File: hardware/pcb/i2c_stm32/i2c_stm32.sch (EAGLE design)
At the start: 41 parts, among them J1 POWER, Q1 16 MHz, Q2 32 MHz, Q3 8 MHz, U1 STM32F103C8T6, U2 MPU-6050, U3 BMP280, U4 NRF24L01

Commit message: Schematic finalized (besides crystal load c ap and resistor values)
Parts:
- removed C14: 10nF, Resistor_Capacitor:C0603C100C5GACTU
- removed C15: 1nF, Resistor_Capacitor:C0603C100C5GACTU
- removed C23: 100 nF, Resistor_Capacitor:C0603C100C5GACTU
- removed J1: POWER, SparkFun-Connectors:CONN_023.5MM
- removed JP1: (no value), adafruit:PINHD-1X6B
- removed JP2: (no value), adafruit:PINHD-1X8BIG
- removed LED1: (no value), led:LED5MM
- removed Q1: 16 MHz, adafruit:CRYSTALHC49S
- removed Q2: 32 MHz, adafruit:CRYSTALHC49S
- removed Q3: 8 MHz, adafruit:CRYSTALHC49S
- removed U$1: 2.7 nH, Nordic_nRF:INDUCTOR_0603_M
- removed U$2: 8.2 nH, Nordic_nRF:INDUCTOR_0603_M
- removed U$3: 3.9 nH, Nordic_nRF:INDUCTOR_0603_M
- added C24: 22nF, Resistor_Capacitor:C0603C100C5GACTU
- added C25, C27, C29: 100nF, Resistor_Capacitor:C0603C100C5GACTU
- added C26: 1uF, Resistor_Capacitor:C0603C100C5GACTU
- added C28: 10uF, Resistor_Capacitor:C0603C100C5GACTU
- added C30, C31: 22pF, Resistor_Capacitor:C0603C100C5GACTU
- added D1, D2: (no value), SparkFun-LED:LED0603
- added J2: (no value), SparkFun-Connectors:CONN_04
- added J3, J4: (no value), SparkFun-Connectors:CONN_20
- added J5: (no value), SparkFun-Connectors:USB_MICRO-B_FEMALE-SMT
- added L1: 2.7 nH, Nordic_nRF:INDUCTOR_0603_M
- added L2: 8.2 nH, Nordic_nRF:INDUCTOR_0603_M
- added L3: 3.9 nH, Nordic_nRF:INDUCTOR_0603_M
- added R4: RC0603JR-070RL, Resistor_Capacitor:RC0603JR-070RL
- added R5: 10k, Resistor_Capacitor:RC0603JR-070RL
- added S1: MOMENTARY-SWITCH-SPST-PTH-6.0MM, SparkFun-Switches:MOMENTARY-SWITCH-SPST-PTH-6.0MM
- added U5: RT9193-33GB, SparkFun-IC-Power:V_REG_MIC5205ADJ
- added Y1: 8MHz, SparkFun-Clocks:CRYSTAL-8MHZSMD-5X3.2
- added Y3: 16MHz, SparkFun-Clocks:CRYSTAL-16MHZSMD-5X3.2
- added Y4: 32.768kHz, SparkFun-Clocks:CRYSTAL-32.768KHZSMD-3.2X1.5
- C10: value 100 nF -> 1pF
- C16, C17: value 2.2nF -> 22pF
- C18, C19: value 2.2nF -> 100nF
- C20, C21: value 100 nF -> 100nF
- C22: value 100 nF -> 1uF
- C4: value 0.01 uF -> 0.01uF
- C9: value 100 nF -> 1.5pF
- R3: value 1 M -> 1M
- U1: SPICEPREFIX (none) -> X
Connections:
- removed net N$10: U$1.1, U$2.1, U4.ANT1
- removed net N$11: U$2.2, U$3.1, U4.ANT2
- removed net SCL: JP1.4, U2.SCL
- removed net SDA: JP1.3, U2.SDA, U3.SDI
- new net 5V: C25.2, C26.2, J4.3, J5.VBUS, U5.EN, U5.IN
- new net ANT1: L1.1, L2.1, U4.ANT1
- new net ANT2: L2.2, L3.1, U4.ANT2
- new net BMP_SCL: U3.BMP_SCK
- new net BMP_SDA: U3.SDI
- new net EP: U2.EP, U4.EP
- new net IMU_SCL: U2.SCL
- new net IMU_SDA: U2.SDA
- new net N$14: C25.1, C26.1, U5.GND
- new net N$15: U3.SDO
- new net OSC32_IN: C30.1, U1.PC14-OSC32_IN, Y4.1
- new net OSC32_OUT: C31.1, U1.PC15-OSC32_OUT, Y4.2
- new net OSC_IN: C16.1, R3.2, U1.PD0_OSC_IN, Y1.1
- new net OSC_OUT: C17.1, R3.1, U1.PD1_OSC_OUT, Y1.2
- new net PA0: J3.5, U1.PA0_WKUP
- new net PA1: J3.6, U1.PA1
- new net PA10: J4.14, U1.PA10
- new net PA11: J4.13, U1.PA11
- new net PA12: J4.12, J4.20, U1.PA12
- new net PA13: J4.19
- new net PA14: J4.18
- new net PA15: J4.11, U1.PA15
- new net PA2: J3.7, U1.PA2
- new net PA3: J3.8, U1.PA3
- new net PA4: J3.9, U1.PA4
- new net PA5: J3.10, U1.PA5
- new net PA6: J3.11, U1.PA6
- new net PA7: J3.12, U1.PA7
- new net PA8: J4.16, U1.PA8
- new net PA9: J4.15, U1.PA9
- new net PB0: J3.13, U1.PB0
- new net PB1: J3.14, U1.PB1
- new net PB10: J3.15, U1.PB10
- new net PB11: J3.16, U1.PB11
- new net PB12: U1.PB12
- new net PB13: U1.PB13
- new net PB14: U1.PB14
- new net PB15: J4.17, U1.PB15
- new net PB2: U1.PB2
- new net PB3: J4.10, U1.PB3
- new net PB4: J4.9, U1.PB4
- new net PB5: J4.8, U1.PB5
- new net PB6: J4.7, U1.PB6
- new net PB7: J4.6, U1.PB7
- new net PB8: J4.5, U1.PB8
- new net PB9: J4.4, U1.PB9
- new net PC13: J3.2, R4.1, U1.PC13-TAMPER-RTC
- new net PC14: J3.3
- new net PC15: J3.4
- new net RESET: C22.1, J3.17, R5.1, S1.1, U1.NRST
- new net SWCLK: J2.2, U1.PA14
- new net SWDIO: J2.3, U1.PA13
- new net VBAT: J3.1, U1.VBAT
- net CE: no longer JP2.3
- net CSN: no longer JP2.4
- net GND: now also C16.2, C17.2, C24.1, C27.2, C28.2, C29.2, C30.2, C31.2, D1.C, D2.C, J2.1, J3.19, J3.20, J4.2, J5.GND, J5.ID, J5.SHIELD, S1.2, U1.BOOT0, U1.VSS, U1.VSSA; no longer C14.2, C15.2, C16.1, C17.1, C23.2, J1.1, JP1.2, JP2.2, LED1.C, U3.SDO
- net IMU_INT: no longer JP1.5
- net IRQ: no longer JP2.8
- net MISO: no longer JP2.7
- net MOSI: no longer JP2.6
- net N$13: now also L3.2; no longer U$3.2
- net N$4: now also D1.A; no longer LED1.A
- net N$5: now also C24.2, U5.BP; no longer Q1.1, U4.XC2
- net N$6: now also D2.A, R4.2; no longer Q1.2, U4.XC1
- net N$7: now also U4.XC2, Y3.1
- net N$8: now also U4.XC1, Y3.2
- net SCK: no longer JP2.5, U3.SCK
- net VDD: now also C18.1, C19.1, C27.1, C28.1, C29.1, J2.4, J3.18, J4.1, R5.2, U1.VDD, U1.VDDA, U5.OUT; no longer C14.1, C15.1, C22.1, C23.1, J1.2, JP1.1, JP2.1
- net VDD_PA: now also L1.2; no longer U$1.2
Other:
- note added: "32.768 kHz Clock"
- note added: "50 Ohm SMT Antenna"
- note added: "5V to 3.3V LDO"
- note added: "8 MHz Clock"
- note added: "BMP280 - Barometer"
- note added: "Debug LED"
- note added: "Headers"
- note added: "I2C 7-bit Address 1101000 (0x68)"
- note added: "I2C 7-bit Address 1110110 (0x76)"
- note added: "J-Link Programmer"
- note added: "LEDs"
- note added: "MCU Power Decoupling"
- note added: "MOSFETs - Motor Controller <TBD>"
- note added: "MPU6050 - 6 DOF IMU"
- note added: "Microcontroller"
- note added: "NRF24 - Radio"
- note added: "Only using for power"
- note added: "Power LED"
- note added: "Reset Switch"
- note added: "SWD"
- note added: "TODO: 1. Confirm capacitor values for crystals (match load capacitance) 2. Create BOM 3. openocd.gdb for debugging 4. Current limiting resistor values for LED 5. Make correct SDA,SCL, and SPI connections 6. Check all values -> Collect all reference material"
- note added: "USB Power Input"
- note removed: "1110110 (0x76)"
- note removed: "ADO LOW -> 1101000"
- note removed: "Bit more than 22pF may be a good idea cause of 18pF load capacitance https://www.digikey.ca/en/products/detail/abracon-llc/ABM3B-16-000MHZ-B2-T/675317"
- note removed: "I WANT TO BE ABLE TO BREAKOUT THE COMPONENTS TO USE WITH ARDUINO FOR TESTING"
- note removed: "I2C Connector"
- note removed: "SPI Connector"
- note removed: "Seperate IMU and BMP I2C channels into I2C1 and I2C2"
- note removed: "TODO: - Add led to pin for testing code upload (blinky) - Create breakout for all pins that are not used - Create boot 3x2 - Create BOM"
- note removed: "VDD + VDDIO can be the same at 3.3V"
- note removed: "use jtag pins bootloader only needed for none-jtag interfaces need openocd.gdb config file for debugging?"

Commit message: schematic updates
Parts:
- removed R4: RC0603JR-070RL, Resistor_Capacitor:RC0603JR-070RL
- added R6: 220, Resistor_Capacitor:RC0603JR-070RL
- C16, C17: value 22pF -> 15pF
- C30, C31: value 22pF -> 10pF
- C7, C8: value 22pF -> 18pF
- R1: value RC0603JR-070RL -> 220
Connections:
- net N$4: now also R6.2; no longer R1.2
- net N$6: now also R1.2; no longer R4.2
- net PC13: now also R1.1; no longer R4.1
- net VDD: now also R6.1; no longer R1.1
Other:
- note added: "C1 = C2 = 2*(CL - CStray) CStray for NRF is ~1pF 2*(10pF - 1pF) = 18pF"
- note added: "C1 = C2 = 2*(CL - CStray) CStray for STM32 is in range [2pF, 7pF] Pick ~ 5pF 2*(10pF - 5pF) = 10pF"
- note added: "C1 = C2 = 2*(CL - CStray) CStray for STM32 is in range [2pF, 7pF] Pick ~ 5pF 2*(12.5pF - 5pF) = 15pF"
- note added: "TODO: 2. Create BOM 3. openocd.gdb for debugging 5. Make correct SDA,SCL, and SPI connections 6. Check all values -> Collect all reference material"
- note removed: "TODO: 1. Confirm capacitor values for crystals (match load capacitance) 2. Create BOM 3. openocd.gdb for debugging 4. Current limiting resistor values for LED 5. Make correct SDA,SCL, and SPI connections 6. Check all values -> Collect all reference material"
- moved on the sheet: R1

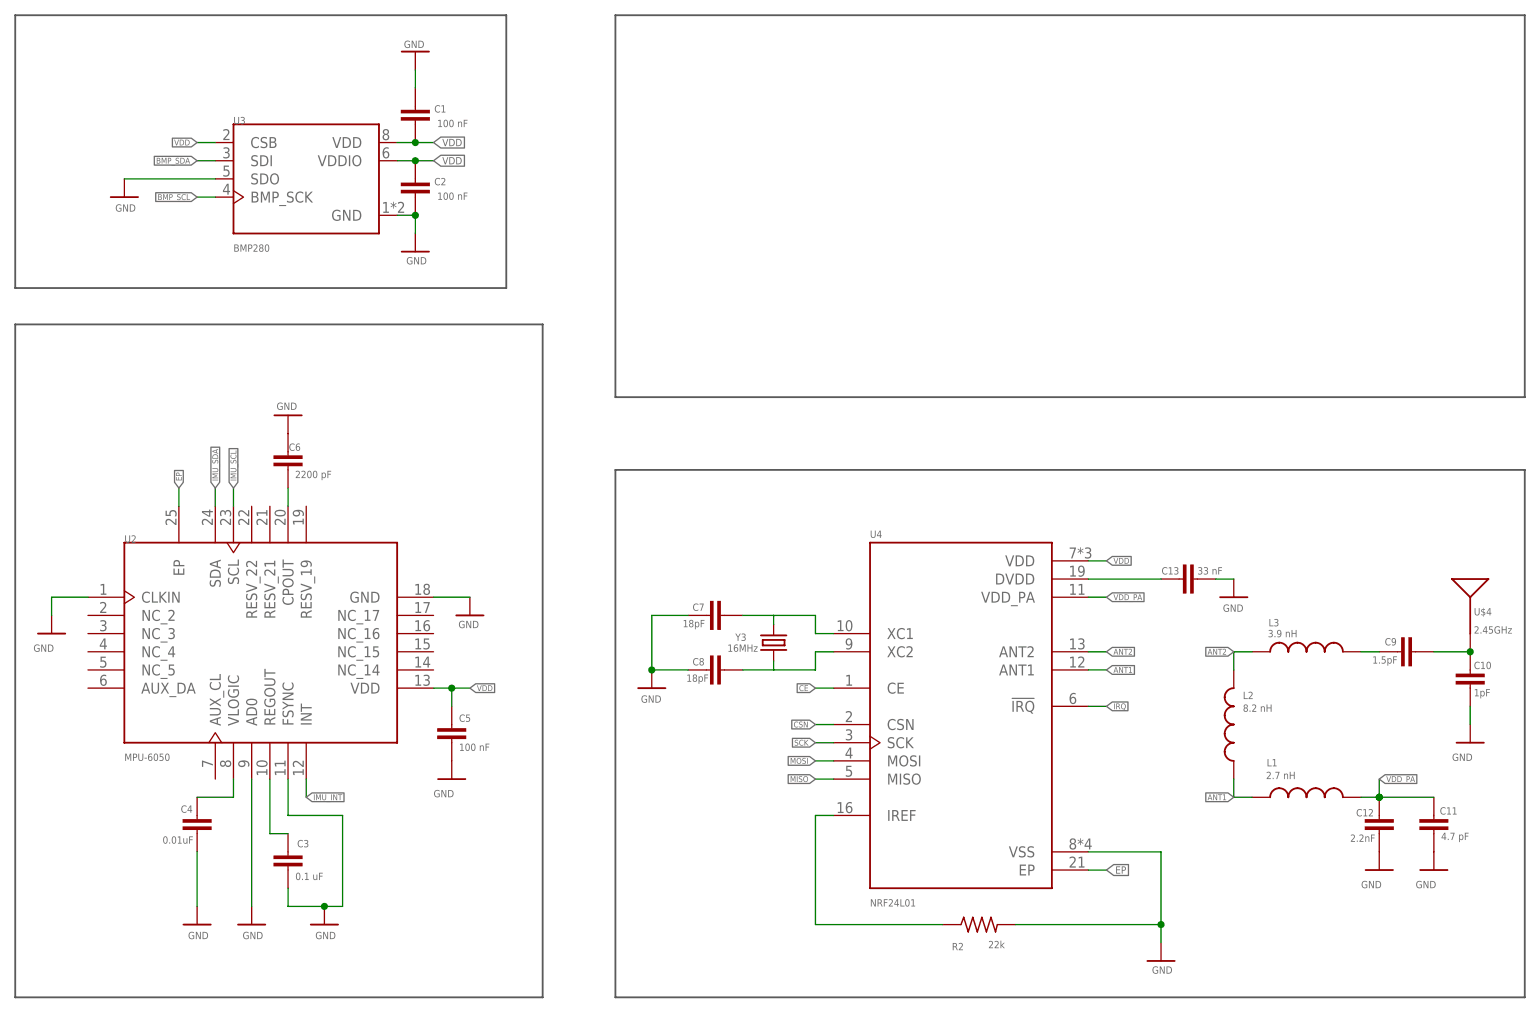
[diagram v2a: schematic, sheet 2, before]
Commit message: Replaced BMP280 w/ BMP388 cause of stock availability and another tweaks to schematic
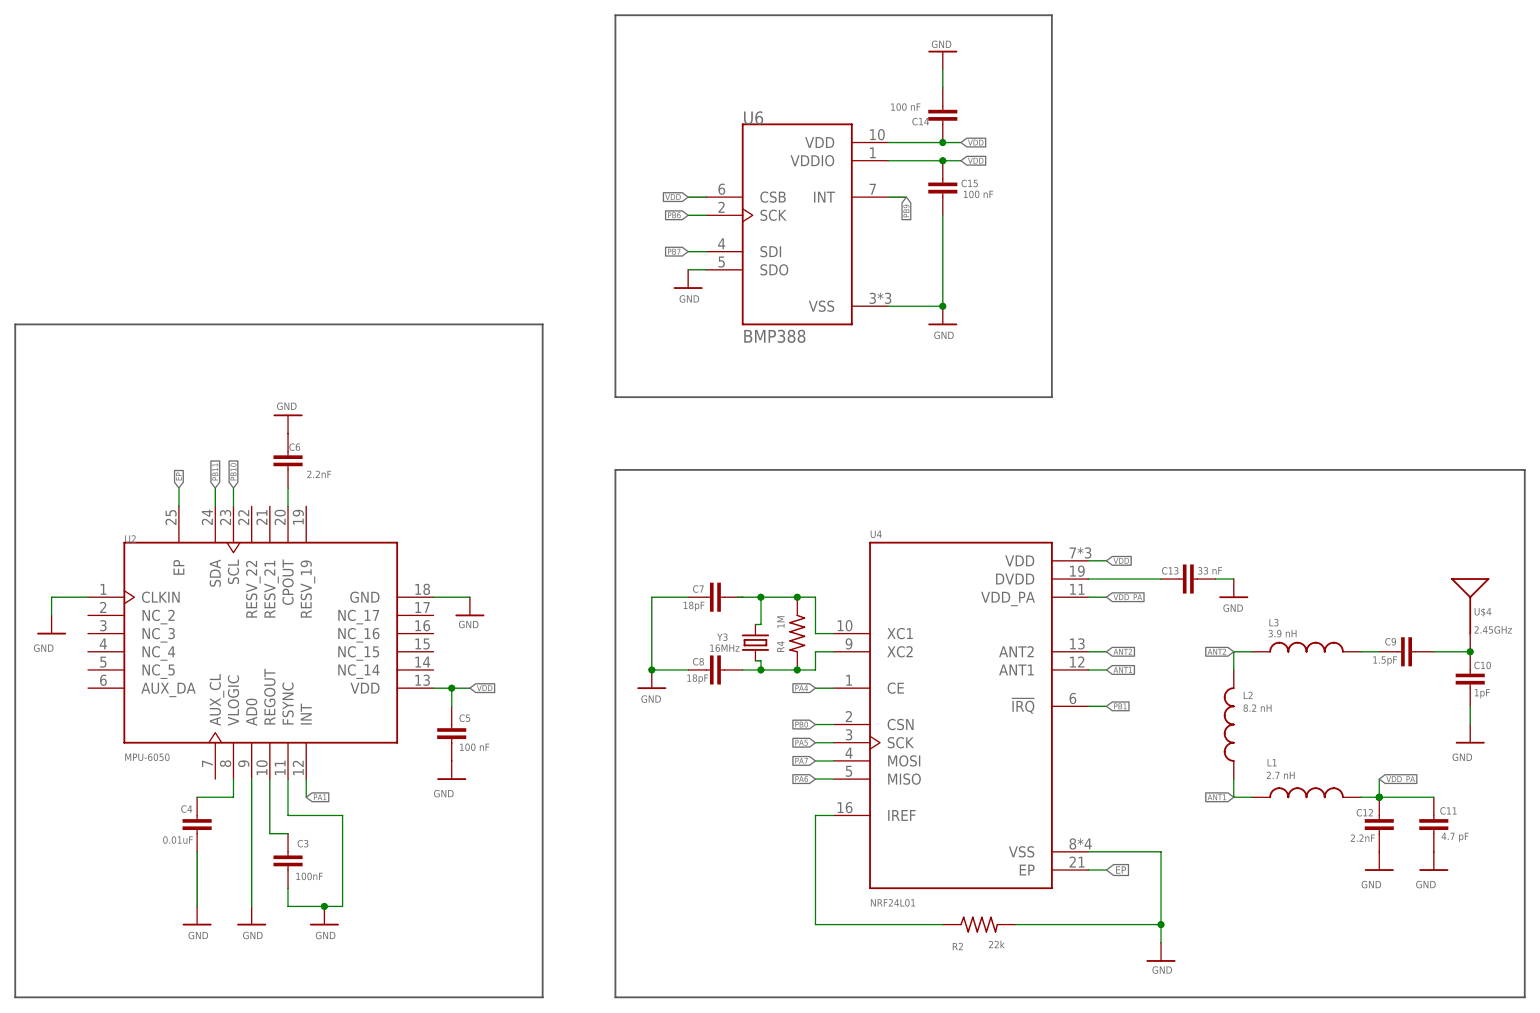
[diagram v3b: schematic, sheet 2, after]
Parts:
- removed C1, C2: 100 nF, Resistor_Capacitor:C0603C100C5GACTU
- removed U3: BMP280, BMP280:BMP280
- added C14, C15: 100 nF, Resistor_Capacitor:C0603C100C5GACTU
- added R10, R7, R8, R9: 4.7k, Resistor_Capacitor:RC0603JR-070RL
- added R4: 1M, Resistor_Capacitor:RC0603JR-070RL
- added U6: BMP388, BMP388:BMP388
- C3: value 0.1 uF -> 100nF
- C6: value 2200 pF -> 2.2nF
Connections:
- removed net BMP_SCL: U3.BMP_SCK
- removed net BMP_SDA: U3.SDI
- removed net CE: U4.CE
- removed net CSN: U4.CSN
- removed net IMU_INT: U2.INT
- removed net IMU_SCL: U2.SCL
- removed net IMU_SDA: U2.SDA
- removed net IRQ: U4.!IRQ
- removed net MISO: U4.MISO
- removed net MOSI: U4.MOSI
- removed net N$15: U3.SDO
- removed net SCK: U4.SCK
- net GND: now also C14.2, C15.1, U6.SDO, U6.VSS; no longer C1.1, C2.2, U3.GND
- net N$7: now also R4.2
- net N$8: now also R4.1
- net PA1: now also U2.INT
- net PA4: now also U4.CE
- net PA5: now also U4.SCK
- net PA6: now also U4.MISO
- net PA7: now also U4.MOSI
- net PB0: now also U4.CSN
- net PB1: now also U4.!IRQ
- net PB10: now also R9.1, U2.SCL
- net PB11: now also R10.1, U2.SDA
- net PB6: now also R7.1, U6.SCK
- net PB7: now also R8.1, U6.SDI
- net PB9: now also U6.INT
- net VDD: now also C14.1, C15.2, R10.2, R7.2, R8.2, R9.2, U6.CSB, U6.VDD, U6.VDDIO; no longer C1.2, C2.1, U3.CSB, U3.VDD, U3.VDDIO
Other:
- note added: "BMP388 - Barometer"
- note added: "I2C Pull Ups"
- note added: "TODO: 2. Validate BOMs 6. Check all values -> Collect all reference material 7. UART connector"
- note removed: "BMP280 - Barometer"
- note removed: "TODO: 2. Create BOM 3. openocd.gdb for debugging 5. Make correct SDA,SCL, and SPI connections 6. Check all values -> Collect all reference material"
- moved on the sheet: C7, Y3

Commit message: Schematic finished, BOM verified
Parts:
- added J1: (no value), SparkFun-Connectors:CONN_04
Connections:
- removed net N$1: C4.1, U2.VLOGIC
- net GND: now also J1.1
- net PA10: now also J1.2
- net PA9: now also J1.3
- net VDD: now also C4.1, J1.4, U2.VLOGIC
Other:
- note added: "RX"
- note added: "TODO: 1. Board design 2. Clean up schematic"
- note added: "TX"
- note added: "UART2"
- note removed: "TODO: 2. Validate BOMs 6. Check all values -> Collect all reference material 7. UART connector"
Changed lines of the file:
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@@
 <part name="C15" library="Resistor_Capacitor" library_urn="urn:adsk.eagle:library:15122775" deviceset="C0603C100C5GACTU" device="" package3d_urn="urn:adsk.eagle:package:10872909/4" value="100 nF"/>
 <part name="GND33" library="supply1" library_urn="urn:adsk.eagle:library:371" deviceset="GND" device=""/>
+<part name="J1" library="SparkFun-Connectors" library_urn="urn:adsk.eagle:library:513" deviceset="CONN_04" device="" package3d_urn="urn:adsk.eagle:package:38085/1"/>
+<part name="GND1" library="supply1" library_urn="urn:adsk.eagle:library:371" deviceset="GND" device=""/>
 </parts>
 <sheets>
@@
 <wire x1="154.94" y1="30.48" x2="215.9" y2="30.48" width="0.254" layer="97"/>
 <wire x1="215.9" y1="30.48" x2="215.9" y2="53.34" width="0.254" layer="97"/>
+<text x="220.98" y="114.3" size="2.54" layer="105" font="vector">UART2</text>
+<wire x1="218.44" y1="119.38" x2="218.44" y2="93.98" width="0.254" layer="97"/>
+<wire x1="218.44" y1="93.98" x2="254" y2="93.98" width="0.254" layer="97"/>
+<wire x1="254" y1="93.98" x2="254" y2="119.38" width="0.254" layer="97"/>
+<wire x1="254" y1="119.38" x2="218.44" y2="119.38" width="0.254" layer="97"/>
+<text x="240.284" y="106.172" size="1.016" layer="105" font="vector">TX</text>
+<text x="240.284" y="103.886" size="1.016" layer="105" font="vector">RX</text>
 </plain>
 <instances>
@@
 <attribute name="NAME" x="195.326" y="38.3286" size="1.016" layer="95" font="vector"/>
 <attribute name="VALUE" x="203.2" y="38.354" size="1.016" layer="96" font="vector"/>
+</instance>
+<instance part="J1" gate="G$1" x="226.06" y="104.14" smashed="yes">
+<attribute name="VALUE" x="220.98" y="96.774" size="1.778" layer="96" font="vector"/>
+<attribute name="NAME" x="220.98" y="112.268" size="1.016" layer="95" font="vector"/>
+</instance>
+<instance part="GND1" gate="1" x="233.68" y="99.06" smashed="yes">
+<attribute name="VALUE" x="231.14" y="96.52" size="1.016" layer="96" font="vector"/>
 </instance>
 </instances>
@@
 <label x="208.026" y="37.338" size="0.8128" layer="95" xref="yes"/>
 </segment>
+<segment>
+<pinref part="J1" gate="G$1" pin="4"/>
+<wire x1="231.14" y1="109.22" x2="233.68" y2="109.22" width="0.1524" layer="91"/>
+<label x="233.68" y="109.22" size="0.8128" layer="95" xref="yes"/>
+</segment>
 </net>
 <net name="GND" class="0">
@@
 <wire x1="190.5" y1="111.76" x2="200.66" y2="111.76" width="0.1524" layer="91"/>
 </segment>
+<segment>
+<pinref part="J1" gate="G$1" pin="1"/>
+<wire x1="231.14" y1="101.6" x2="233.68" y2="101.6" width="0.1524" layer="91"/>
+<pinref part="GND1" gate="1" pin="GND"/>
+</segment>
 </net>
 <net name="N$4" class="0">
@@
 <label x="198.12" y="78.74" size="0.8128" layer="95" font="vector" rot="R180" xref="yes"/>
 </segment>
+<segment>
+<pinref part="J1" gate="G$1" pin="3"/>
+<wire x1="231.14" y1="106.68" x2="233.68" y2="106.68" width="0.1524" layer="91"/>
+<label x="233.68" y="106.68" size="0.8128" layer="95" xref="yes"/>
+</segment>
 </net>
 <net name="PA10" class="0">
@@
 <wire x1="200.66" y1="81.28" x2="198.12" y2="81.28" width="0.1524" layer="91"/>
 <label x="198.12" y="81.28" size="0.8128" layer="95" font="vector" rot="R180" xref="yes"/>
+</segment>
+<segment>
+<pinref part="J1" gate="G$1" pin="2"/>
+<wire x1="231.14" y1="104.14" x2="233.68" y2="104.14" width="0.1524" layer="91"/>
+<label x="233.68" y="104.14" size="0.8128" layer="95" xref="yes"/>
 </segment>
 </net>
@@
 <label x="121.92" y="139.7" size="0.8128" layer="95" rot="R180" xref="yes"/>
 </segment>
+<segment>
+<pinref part="U2" gate="G$1" pin="VLOGIC"/>
+<wire x1="58.42" y1="58.42" x2="58.42" y2="55.88" width="0.1524" layer="91"/>
+<wire x1="58.42" y1="55.88" x2="53.34" y2="55.88" width="0.1524" layer="91"/>
+<pinref part="C4" gate="G$1" pin="1"/>
+<wire x1="53.34" y1="55.88" x2="48.26" y2="55.88" width="0.1524" layer="91"/>
+<junction x="53.34" y="55.88"/>
+<label x="48.26" y="55.88" size="0.8128" layer="95" rot="R180" xref="yes"/>
+</segment>
 </net>
 <net name="GND" class="0">
@@
 <wire x1="63.5" y1="50.8" x2="66.04" y2="50.8" width="0.1524" layer="91"/>
 <pinref part="C3" gate="G$1" pin="1"/>
-</segment>
-</net>
-<net name="N$1" class="0">
-<segment>
-<pinref part="U2" gate="G$1" pin="VLOGIC"/>
-<wire x1="58.42" y1="58.42" x2="58.42" y2="55.88" width="0.1524" layer="91"/>
-<wire x1="58.42" y1="55.88" x2="53.34" y2="55.88" width="0.1524" layer="91"/>
-<pinref part="C4" gate="G$1" pin="1"/>
 </segment>
 </net>
@@
 <plain>
 <text x="15.24" y="27.94" size="5.08" layer="105" font="vector">TODO:
-2. Validate BOMs
-6. Check all values -&gt; Collect all reference material
-7. UART connector</text>
+1. Board design
+2. Clean up schematic</text>
 </plain>
 <instances>

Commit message: finalized circuit boards and ordered w/ gerber files
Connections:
- removed net N$14: C25.1, C26.1, U5.GND
- removed net PA13: J4.19
- removed net PA14: J4.18
- removed net PB2: U1.PB2
- removed net VBAT: J3.1, U1.VBAT
- net GND: now also C25.1, C26.1, U1.PB2, U5.GND
- net PA1: no longer U2.INT
- net PA12: no longer J4.20
- net PB12: now also J4.20
- net PB13: now also J4.19
- net PB14: now also J4.18
- net PB9: no longer U6.INT
